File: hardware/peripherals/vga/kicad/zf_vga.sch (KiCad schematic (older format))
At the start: 35 parts

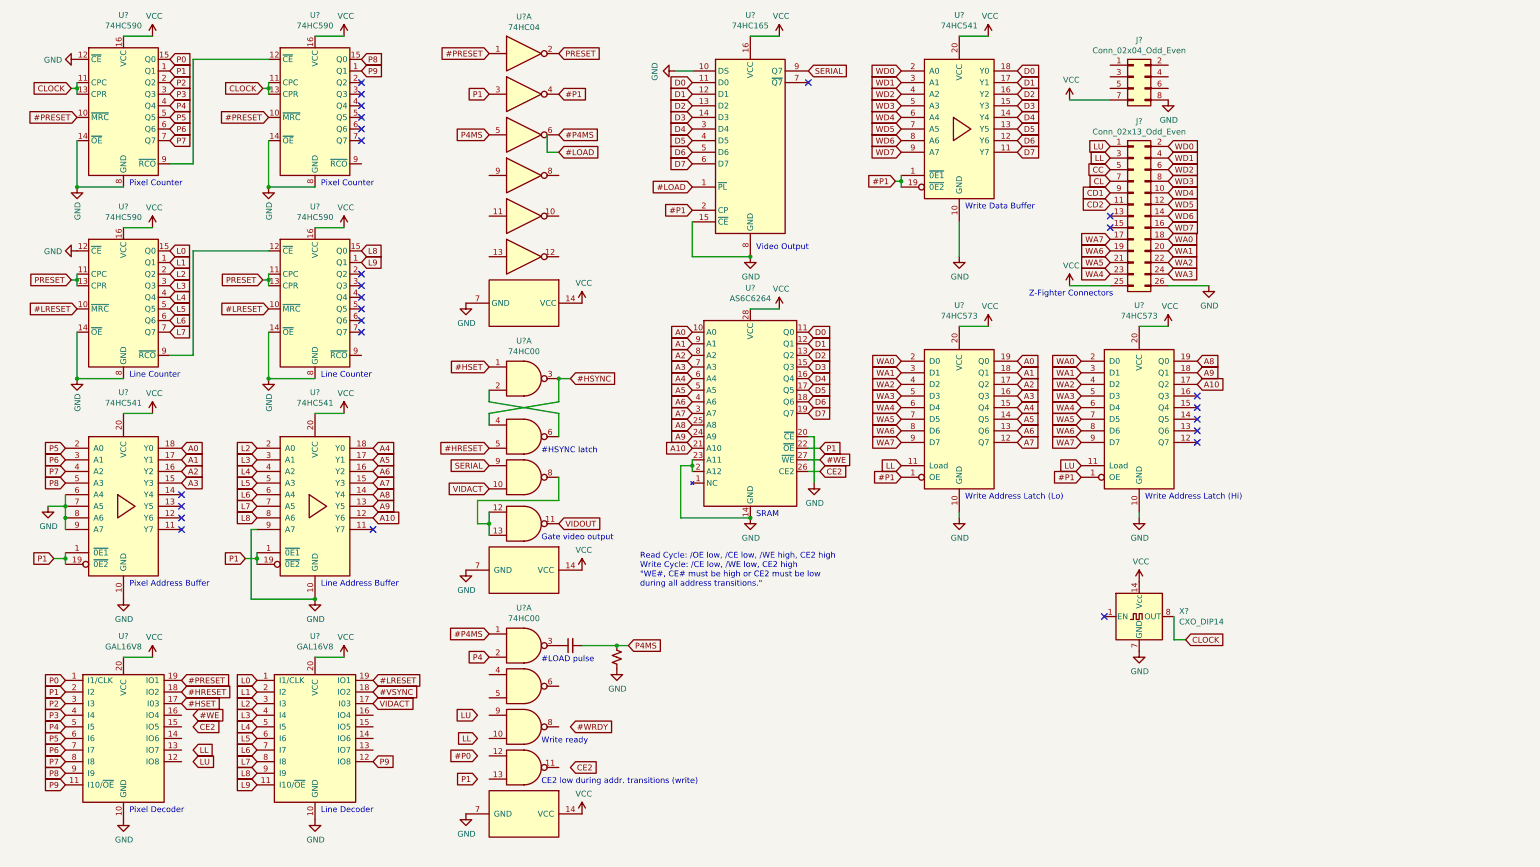
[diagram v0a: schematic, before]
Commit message: VRAM sharing, write timing
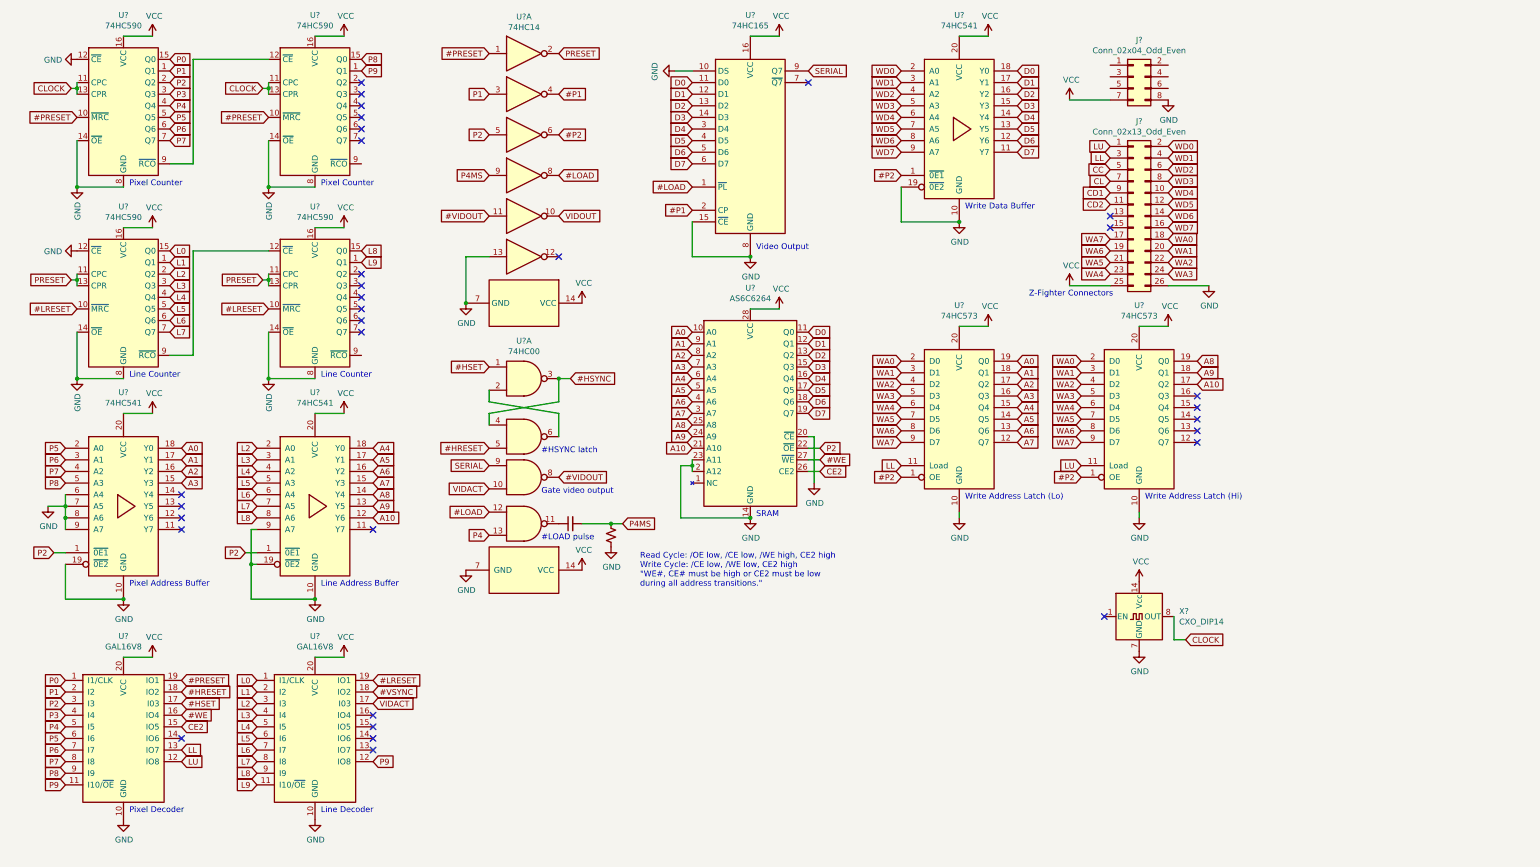
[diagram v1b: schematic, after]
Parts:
- removed U? (x5): 74HC00, symbol 74xx:74HC00
- U?: value 74HC04 -> 74HC14
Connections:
- net #LOAD: now also U?.12, U?.8
- net #P1: no longer U?.1 (OE), U?.1 (OE), U?.1 (~0E1), U?.19 (~0E2)
- net #WE: now also U?.16 (IO4)
- net CE2: now also U?.15 (IO5)
- net GND: now also U?.13, U?.19 (~0E2), U?.19 (~0E2), U?.19 (~0E2)
- net LL: now also U?.13 (IO7)
- net LU: now also U?.12 (IO8)
- net P1: no longer U?.1 (~0E1), U?.1 (~0E1), U?.19 (~0E2), U?.19 (~0E2), U?.22 (~OE)
- net P2: now also U?.1 (~0E1), U?.1 (~0E1), U?.22 (~OE), U?.5
- net P4: now also U?.13
- net P4MS: now also U?.9; no longer U?.5
- net VIDOUT: now also U?.10; no longer U?.11
- net #VIDOUT: now reaches U?.11
- net #VIDOUT: now also U?.8
- net at C?.1: now also U?.11
- net #P4MS renamed #P2
- net #P2: now also U?.1 (OE), U?.1 (OE), U?.1 (~0E1)
- no-connect marks 26 -> 32
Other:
- note removed: "CE2 low during addr. transitions (write)"
- note removed: "Write ready"

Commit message: Working design!
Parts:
- added U? (x3): 74HC74, symbol 74xx:74HC74
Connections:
- net #HSYNC: now also U?.5 (Q); no longer U?.3, U?.4
- net GND: now also U?.10, U?.12, U?.13, U?.9, U?.7 (GND); no longer U?.13
- net LL: now also U?.5; no longer U?.13 (IO7)
- net LU: now also U?.4; no longer U?.12 (IO8)
- net P1: now also U?.12 (IO8); no longer U?.3
- net P2: now also U?.11 (C); no longer U?.1 (~0E1), U?.1 (~0E1), U?.22 (~OE), U?.5
- net P4: now also U?.13 (IO7); no longer U?.13
- net P4MS: now also U?.3; no longer U?.9
- net P9: now also U?.14 (IO6); no longer U?.12 (IO8)
- net VCC: now also U?.1 (~R), U?.10 (~S), U?.13 (~R), U?.14 (VCC), U?.4 (~S)
- net VIDOUT: now also U?.9 (Q7); no longer U?.10
- net BUS: now reaches U?.14 (IO6)
- net BUS: now also U?.1 (~0E1), U?.1 (~0E1), U?.5
- net #LDPULSE: now reaches U?.2
- net #LDPULSE: now also U?.1 (~PL), U?.4; no longer U?.6
- net at C?.1: now also U?.3; no longer U?.11
- net SCLOCK: now reaches U?.16 (IO4)
- net SCLOCK: now also U?.2 (CP)
- net #HRESET renamed HPULSE
- net HPULSE: now also U?.3 (C); no longer U?.5
- net #HSET renamed #LD
- net #LD: now also U?.17 (I03); no longer U?.17 (I03)
- removed net #LOAD: U?.1 (~PL), U?.12, U?.8
- removed net #P1: U?.2 (CP), U?.4
- net #P2 renamed #BUS
- net #VIDOUT: no longer names the net of U?.8
- net #VIDOUT: no longer U?.11
- removed net SERIAL: U?.9, U?.9 (Q7)
- removed net VIDACT: U?.10, U?.17 (I03)
- new net: U?.2 (D), U?.6 (~Q)
- new net #LULL: U?.12 (D), U?.6
- new net #OE: U?.17 (I03), U?.22 (~OE)
- new net #WRDY: U?.12 (IO8), U?.9 (Q)
- no-connect marks 32 -> 39
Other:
- note added: "Data ready"
- note added: "H Decoder"
- note added: "V Decoder"
- note added: "Write ready"
- note added: "~HSYNC"
- note removed: "#HSYNC latch"
- note removed: "Gate video output"
- note removed: "Line Decoder"
- note removed: "Pixel Decoder"
- note removed: "Read Cycle: /OE low, /CE low, /WE high, CE2 high\nWrite Cycle: /CE low, /WE low, CE2 high\n"WE#, CE# must be high or CE2 must be low\nduring all address transitions.""
- moved on the sheet: U?A

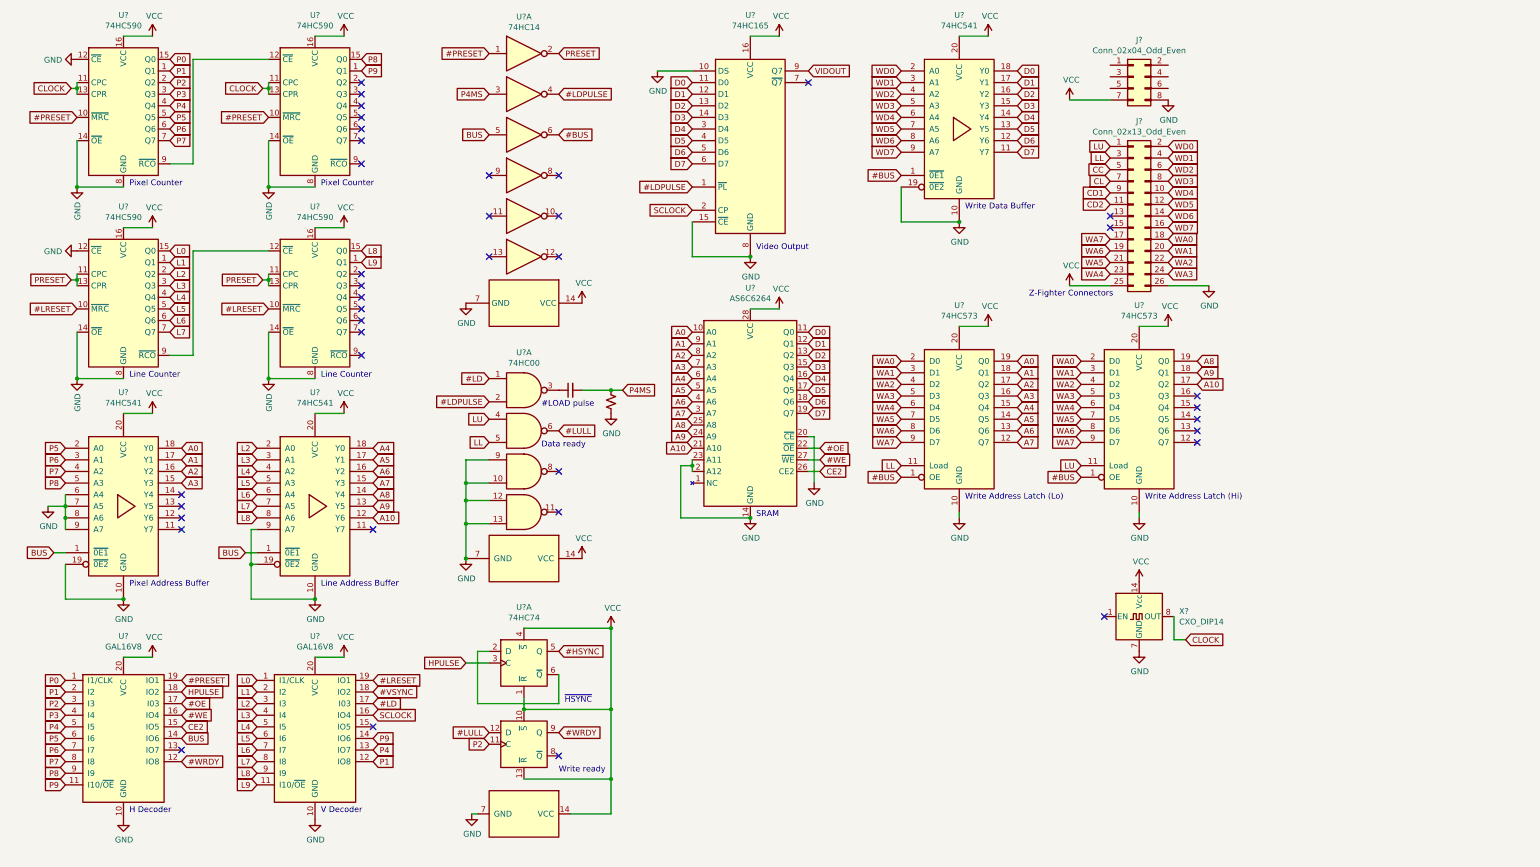
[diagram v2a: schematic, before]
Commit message: Replaced write address latches with buffers
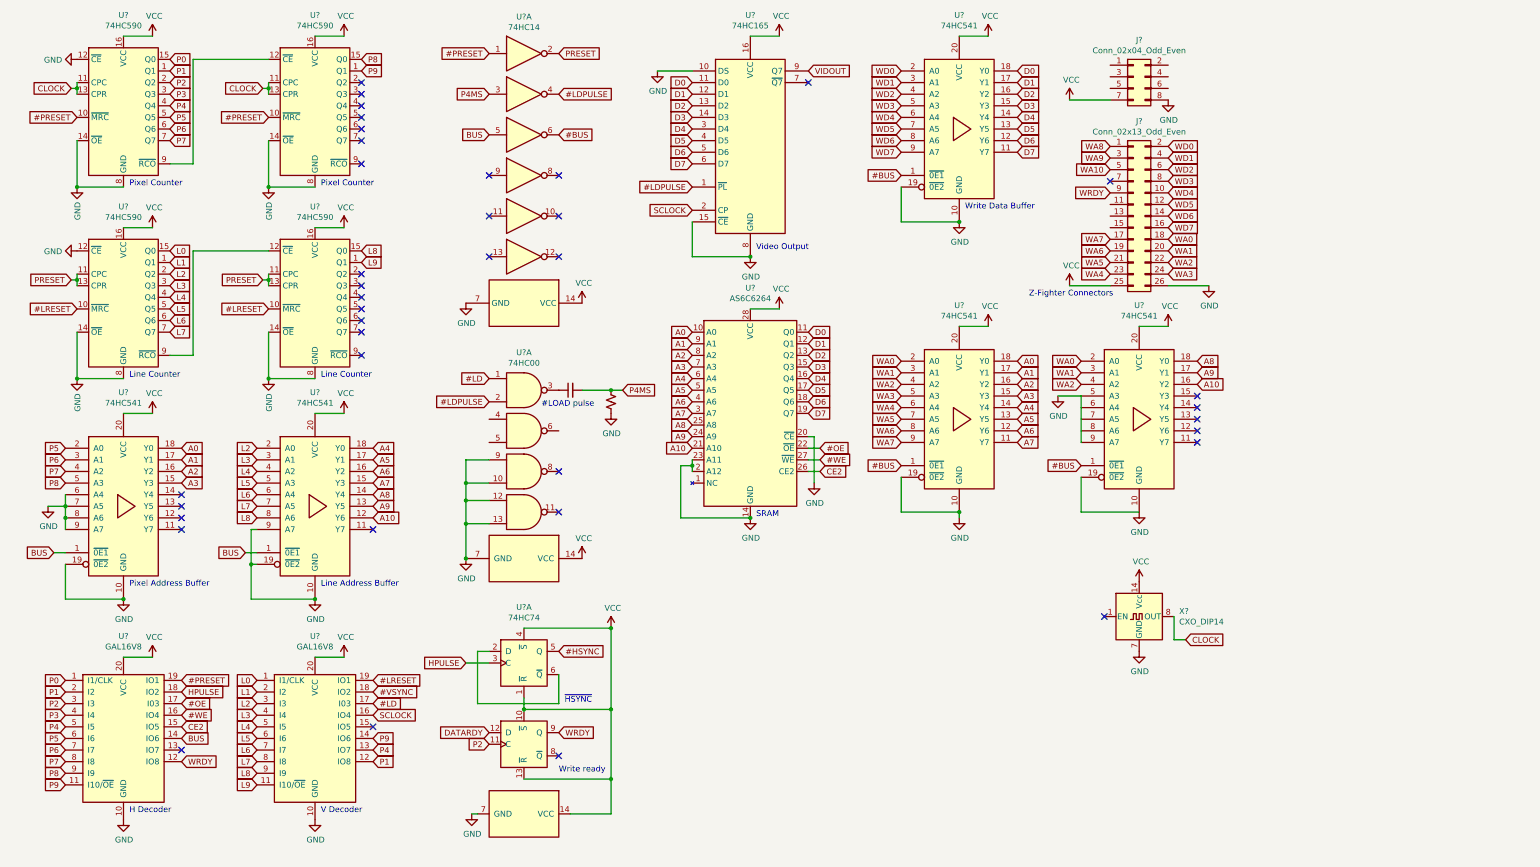
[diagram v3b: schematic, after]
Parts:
- removed U? (x2): 74HC573, symbol 74xx:74LS573
- added U? (x2): 74HC541, symbol 74xx:74HC541
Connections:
- net CD1 is gone; now on net WRDY: J?.9 (Pin_9)
- net #BUS: now also U?.1 (~0E1), U?.1 (~0E1)
- net A0: now also U?.18 (Y0)
- net A1: now also U?.17 (Y1)
- net A10: now also U?.16 (Y2)
- net A2: now also U?.16 (Y2)
- net A3: now also U?.15 (Y3)
- net A4: now also U?.14 (Y4)
- net A5: now also U?.13 (Y5)
- net A6: now also U?.12 (Y6)
- net A7: now also U?.11 (Y7)
- net A8: now also U?.18 (Y0)
- net A9: now also U?.17 (Y1)
- net GND: now also U?.10 (GND), U?.10 (GND), U?.19 (~0E2), U?.19 (~0E2), U?.5 (A3), U?.9 (A7)
- net VCC: now also U?.20 (VCC), U?.20 (VCC)
- net WA0: now also U?.2 (A0), U?.2 (A0)
- net WA1: now also U?.3 (A1), U?.3 (A1)
- net WA2: now also U?.4 (A2), U?.4 (A2)
- net WA3: now also U?.5 (A3)
- net WA4: now also U?.6 (A4)
- net WA5: now also U?.7 (A5)
- net WA6: now also U?.8 (A6)
- net WA7: now also U?.9 (A7)
- net #LULL: no longer names the net of U?.6
- net #LULL: no longer U?.12 (D)
- net #WRDY renamed WRDY
- net CC renamed WA10
- net CD2: no longer names the net of J?.11 (Pin_11)
- net CL: no longer names the net of J?.7 (Pin_7)
- net LL: no longer names the net of U?.5
- net LL: no longer J?.3 (Pin_3)
- net LU: no longer names the net of U?.4
- net LU: no longer J?.1 (Pin_1)
- new net DATARDY: U?.12 (D)
- new net WA8: J?.1 (Pin_1)
- new net WA9: J?.3 (Pin_3)
- no-connect marks 39 -> 38
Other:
- note removed: "Data ready"
- note removed: "Write Address Latch (Hi)"
- note removed: "Write Address Latch (Lo)"
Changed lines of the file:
@@
 Text Notes 8700 2250 0    50   ~ 0
 Write Data Buffer
-$Comp
-L power:GND #PWR0135
-U 1 1 622D4D53
-P 10200 4900
-F 0 "#PWR0135" H 10200 4650 50  0001 C CNN
-F 1 "GND" H 10205 4727 50  0000 C CNN
-F 2 "" H 10200 4900 50  0001 C CNN
-F 3 "" H 10200 4900 50  0001 C CNN
-	1    10200 4900
-	1    0    0    -1
-$EndComp
-Text Notes 10250 4750 0    50   ~ 0
-Write Address Latch (Hi)
 Text Notes 3150 3700 0    50   ~ 0
 Line Counter
@@
 Text GLabel 10450 2700 2    50   Input ~ 0
 WA2
-$Comp
-L 74xx:74LS573 U?
-U 1 1 622882D1
-P 10200 4050
-F 0 "U?" H 10200 5031 50  0000 C CNN
-F 1 "74HC573" H 10200 4940 50  0000 C CNN
-F 2 "" H 10200 4050 50  0001 C CNN
-F 3 "74xx/74hc573.pdf" H 10200 4050 50  0001 C CNN
-	1    10200 4050
-	1    0    0    -1
-$EndComp
 Text GLabel 9950 2500 0    50   Input ~ 0
 WA7
@@
 Text GLabel 9950 2600 0    50   Input ~ 0
 WA6
-Text GLabel 9700 4150 0    50   Input ~ 0
-WA6
-Text GLabel 9700 4050 0    50   Input ~ 0
-WA5
-Text GLabel 9700 3950 0    50   Input ~ 0
-WA4
-Text GLabel 9700 4250 0    50   Input ~ 0
-WA7
-Text GLabel 9700 3850 0    50   Input ~ 0
-WA3
 Text GLabel 9700 3550 0    50   Input ~ 0
 WA0
@@
 Text GLabel 9700 3750 0    50   Input ~ 0
 WA2
-Text GLabel 9950 1800 0    50   Input ~ 0
-LL
-Text GLabel 9950 1700 0    50   Input ~ 0
-LU
 $Comp
 L power:VCC #PWR0139
@@
 Text GLabel 3600 6500 2    50   Input ~ 0
 #LD
-Text GLabel 9700 4450 0    50   Input ~ 0
-LU
-Text GLabel 9950 1900 0    50   Input ~ 0
-CC
-Text GLabel 9950 2000 0    50   Input ~ 0
-CL
-Text GLabel 9950 2100 0    50   Input ~ 0
-CD1
-Text GLabel 9950 2200 0    50   Input ~ 0
-CD2
-Text GLabel 8150 4450 0    50   Input ~ 0
-LL
 Text GLabel 8150 4250 0    50   Input ~ 0
 WA7
@@
 	1    0    0    -1
 $EndComp
-Wire Wire Line
-	8650 3250 8900 3250
 Text GLabel 9150 3750 2    50   Input ~ 0
 A2
@@
 	1    0    0    -1
 $EndComp
-Text Notes 8700 4750 0    50   ~ 0
-Write Address Latch (Lo)
-$Comp
-L 74xx:74LS573 U?
-U 1 1 622253F3
-P 8650 4050
-F 0 "U?" H 8650 5031 50  0000 C CNN
-F 1 "74HC573" H 8650 4940 50  0000 C CNN
-F 2 "" H 8650 4050 50  0001 C CNN
-F 3 "74xx/74hc573.pdf" H 8650 4050 50  0001 C CNN
-	1    8650 4050
-	1    0    0    -1
-$EndComp
 Wire Wire Line
 	6250 4450 6250 4900
@@
 Wire Wire Line
 	10200 3250 10450 3250
-Wire Wire Line
-	8650 4900 8650 4850
-Wire Wire Line
-	10200 4850 10200 4900
 NoConn ~ 10700 3850
 NoConn ~ 10700 3950
@@
 Text Notes 9250 3000 0    50   ~ 0
 Z-Fighter Connectors
-NoConn ~ 9950 2300
-NoConn ~ 9950 2400
 $Comp
 L 74xx:74HC00 U?
@@
 Text GLabel 4600 1250 0    50   Input ~ 0
 P4MS
-Text GLabel 4600 4050 0    50   Input ~ 0
-LU
-Text GLabel 4600 4250 0    50   Input ~ 0
-LL
 $Comp
 L 74xx:74HC04 U?
@@
 Text GLabel 2500 5200 0    50   Input ~ 0
 BUS
-Text GLabel 8150 4550 0    50   Input ~ 0
+Text GLabel 8150 4450 0    50   Input ~ 0
 #BUS
-Text GLabel 9700 4550 0    50   Input ~ 0
+Text GLabel 9700 4450 0    50   Input ~ 0
 #BUS
 Text GLabel 8150 1950 0    50   Input ~ 0
@@
 Wire Wire Line
 	6350 2650 6350 2350
-Text GLabel 5200 4150 2    50   Input ~ 0
-#LULL
 Text GLabel 6350 2050 0    50   Input ~ 0
 #LDPULSE
@@
 NoConn ~ 3500 1850
 Text GLabel 1950 7000 2    50   Input ~ 0
-#WRDY
+WRDY
 Text GLabel 3600 6600 2    50   Input ~ 0
 SCLOCK
@@
 Text GLabel 4600 6850 0    50   Input ~ 0
 P2
-Text GLabel 4600 6750 0    50   Input ~ 0
-#LULL
 Text GLabel 5200 6750 2    50   Input ~ 0
-#WRDY
+WRDY
 Text GLabel 1950 6300 2    50   Input ~ 0
 #PRESET
@@
 NoConn ~ 5200 4500
 NoConn ~ 5200 4850
-Text Notes 5050 4300 0    50   ~ 0
-Data ready
 Text Notes 5200 7100 0    50   ~ 0
 Write ready
@@
 #HSYNC
 NoConn ~ 1950 6900
+$Comp
+L power:GND #PWR?
+U 1 1 622324B0
+P 9500 3850
+F 0 "#PWR?" H 9500 3600 50  0001 C CNN
+F 1 "GND" H 9505 3677 50  0000 C CNN
+F 2 "" H 9500 3850 50  0001 C CNN
+F 3 "" H 9500 3850 50  0001 C CNN
+	1    9500 3850
+	1    0    0    -1
+$EndComp
+Wire Wire Line
+	9500 3850 9700 3850
+Wire Wire Line
+	9700 3850 9700 4250
+$Comp
+L 74xx:74HC541 U?
+U 1 1 62245D6C
+P 10200 4050
+F 0 "U?" H 10200 5031 50  0000 C CNN
+F 1 "74HC541" H 10200 4940 50  0000 C CNN
+F 2 "" H 10200 4050 50  0001 C CNN
+F 3 "http://www.ti.com/lit/gpn/sn74LS245" H 10200 4050 50  0001 C CNN
+	1    10200 4050
+	1    0    0    -1
+$EndComp
+Text GLabel 9950 1700 0    50   Input ~ 0
+WA8
+Text GLabel 9950 1800 0    50   Input ~ 0
+WA9
+Text GLabel 9950 1900 0    50   Input ~ 0
+WA10
+NoConn ~ 9950 2000
+Text GLabel 9950 2100 0    50   Input ~ 0
+WRDY
+Text GLabel 4600 6750 0    50   Input ~ 0
+DATARDY
+Wire Wire Line
+	8650 3250 8900 3250
+Wire Wire Line
+	8650 4900 8650 4850
+$Comp
+L 74xx:74HC541 U?
+U 1 1 62242671
+P 8650 4050
+F 0 "U?" H 8650 5031 50  0000 C CNN
+F 1 "74HC541" H 8650 4940 50  0000 C CNN
+F 2 "" H 8650 4050 50  0001 C CNN
+F 3 "http://www.ti.com/lit/gpn/sn74LS245" H 8650 4050 50  0001 C CNN
+	1    8650 4050
+	1    0    0    -1
+$EndComp
+Wire Wire Line
+	8150 4550 8150 4850
+Wire Wire Line
+	8150 4850 8650 4850
+Connection ~ 8650 4850
+Wire Wire Line
+	9700 4550 9700 4850
+Wire Wire Line
+	9700 4850 10200 4850
+$Comp
+L power:GND #PWR?
+U 1 1 6228001F
+P 10200 4850
+F 0 "#PWR?" H 10200 4600 50  0001 C CNN
+F 1 "GND" H 10205 4677 50  0000 C CNN
+F 2 "" H 10200 4850 50  0001 C CNN
+F 3 "" H 10200 4850 50  0001 C CNN
+	1    10200 4850
+	1    0    0    -1
+$EndComp
 $EndSCHEMATC
